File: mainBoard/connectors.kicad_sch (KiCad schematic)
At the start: 27 parts, among them J11 Conn_01x04, J12 Conn_01x05, J13 Conn_01x04, J14 Conn_01x06, J15 Conn_01x08, J16 Conn_01x03, J6 Conn_01x07, J7 Conn_01x04, J8 Conn_01x02, J9 Conn_01x02, Q2 IRLML6244TRPBF, Q3 IRLML6244TRPBF, Q4 IRLML6244TRPBF, Q5 IRLML6244TRPBF

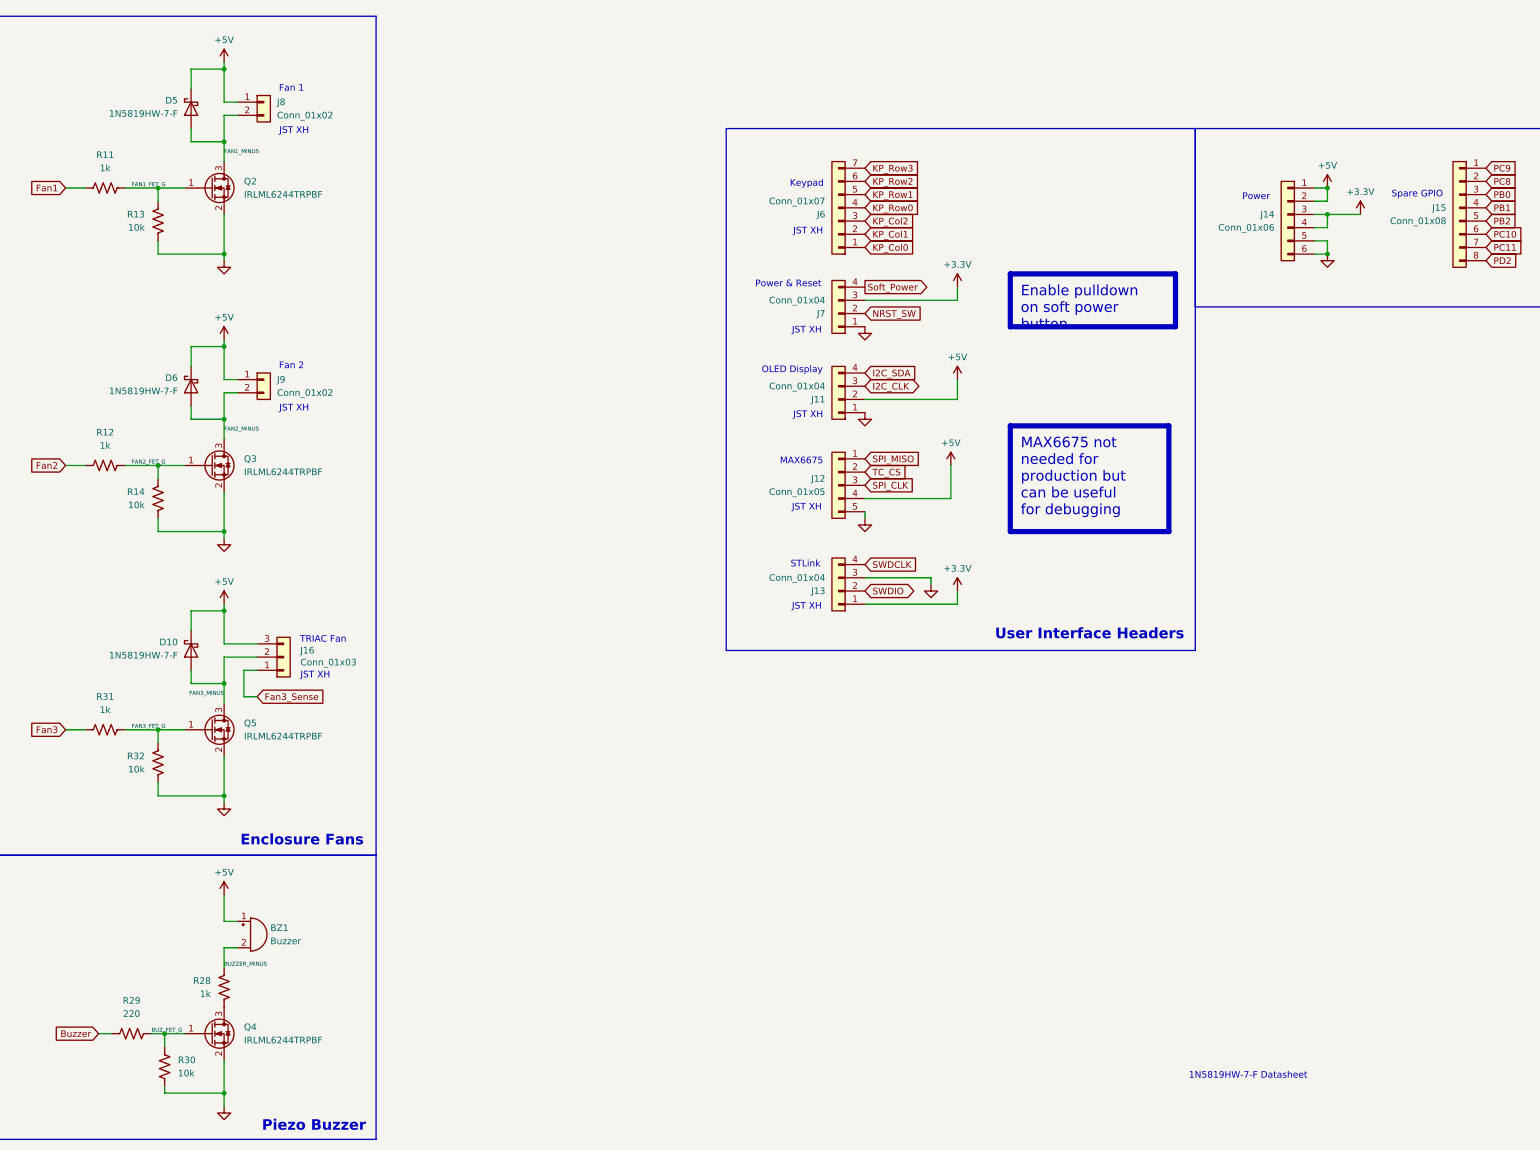
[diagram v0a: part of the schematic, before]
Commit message: Schematic Capture should be complete, ready for PCB
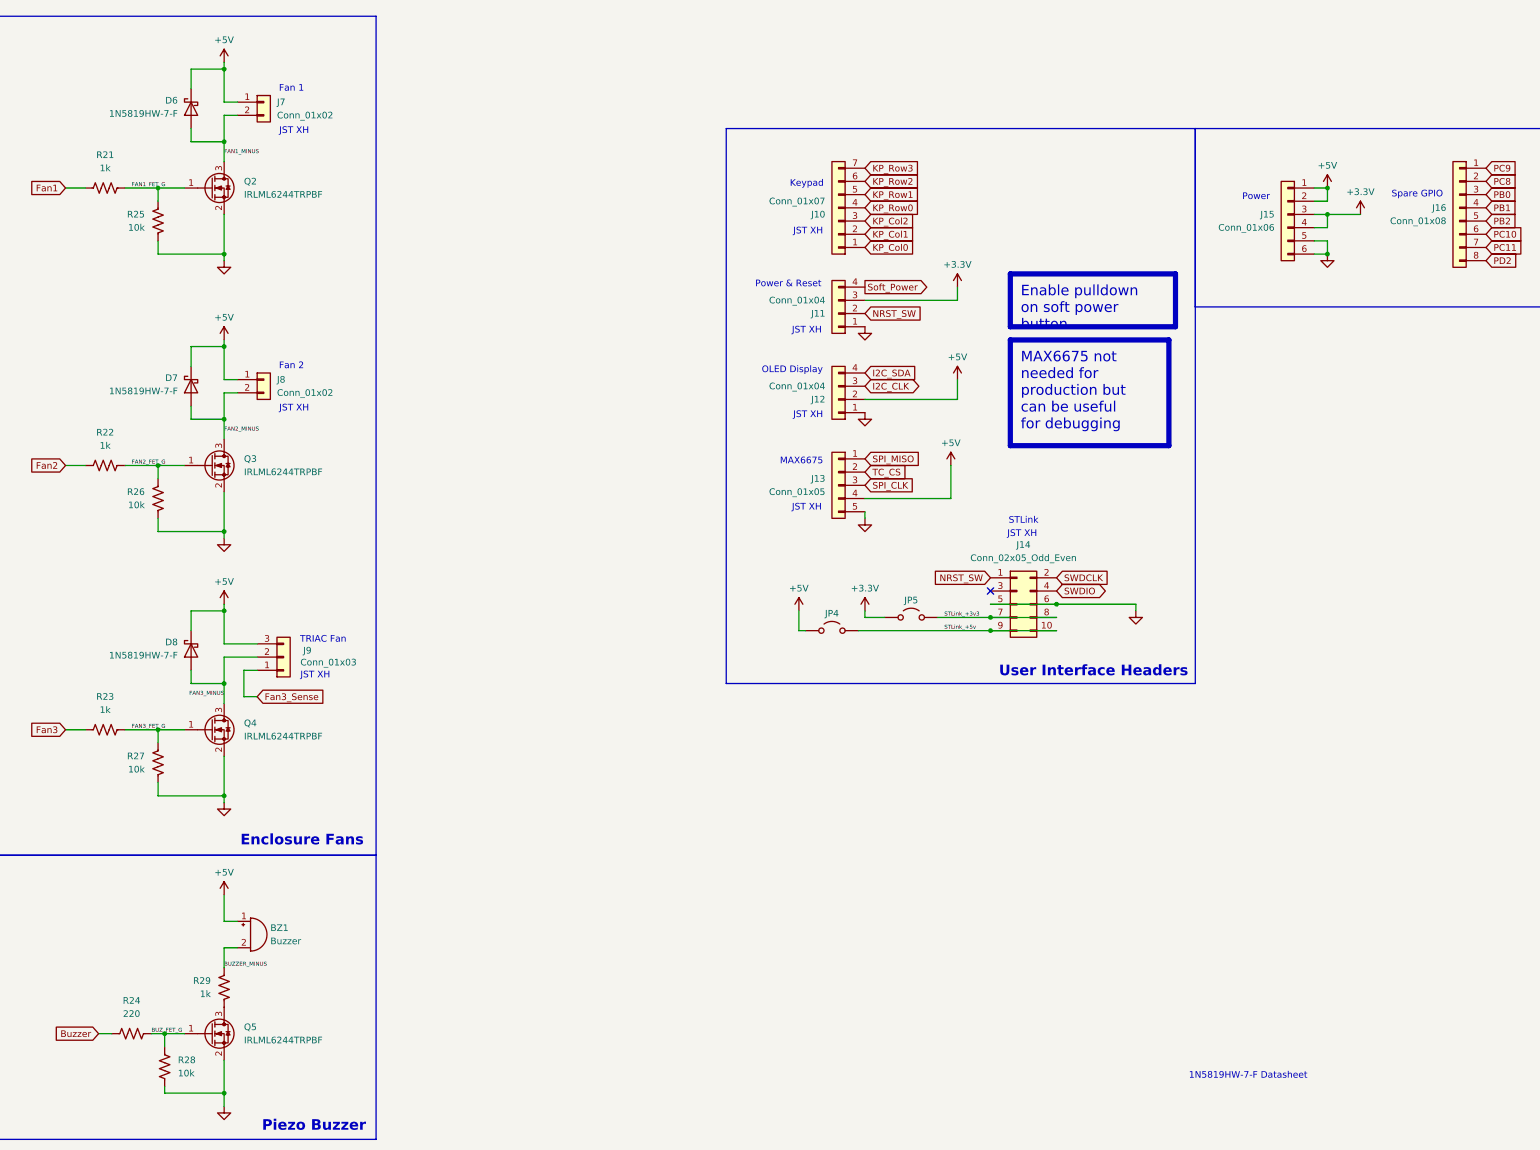
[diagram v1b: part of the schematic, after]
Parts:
- removed J13: Conn_01x04, Connector_JST:JST_XH_B4B-XH-A_1x04_P2.50mm_Vertical, symbol Connector_Generic:Conn_01x04
- added J14: Conn_02x05_Odd_Even, Connector_IDC:IDC-Header_2x05_P2.54mm_Vertical, symbol Connector_Generic:Conn_02x05_Odd_Even
- added JP4, JP5: Jumper_2_Open, Jumper:SolderJumper-2_P1.3mm_Open_TrianglePad1.0x1.5mm, symbol Jumper:Jumper_2_Open
- renumbered D5 to D6, D6 to D7, D10 to D8, J6 to J10, J7 to J11, J11 to J12, J12 to J13, J14 to J15, J15 to J16, J8 to J7, J9 to J8, J16 to J9, Q5 to Q4, Q4 to Q5, R11 to R21, R12 to R22, R31 to R23, R29 to R24, R13 to R25, R14 to R26, R32 to R27, R30 to R28, R28 to R29
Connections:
- net +3.3V: now also JP5.1 (A)
- net +5V: now also JP4.1 (A)
- net GND: now also J14.5 (Pin_5), J14.6 (Pin_6)
- net NRST_SW: now also J14.1 (Pin_1)
- net SWDCLK: now also J14.2 (Pin_2)
- net SWDIO: now also J14.4 (Pin_4)
- new net STLink_+3v3: J14.7 (Pin_7), J14.8 (Pin_8), JP5.2 (B)
- new net STLink_+5v: J14.10 (Pin_10), J14.9 (Pin_9), JP4.2 (B)
- no-connect marks 0 -> 1

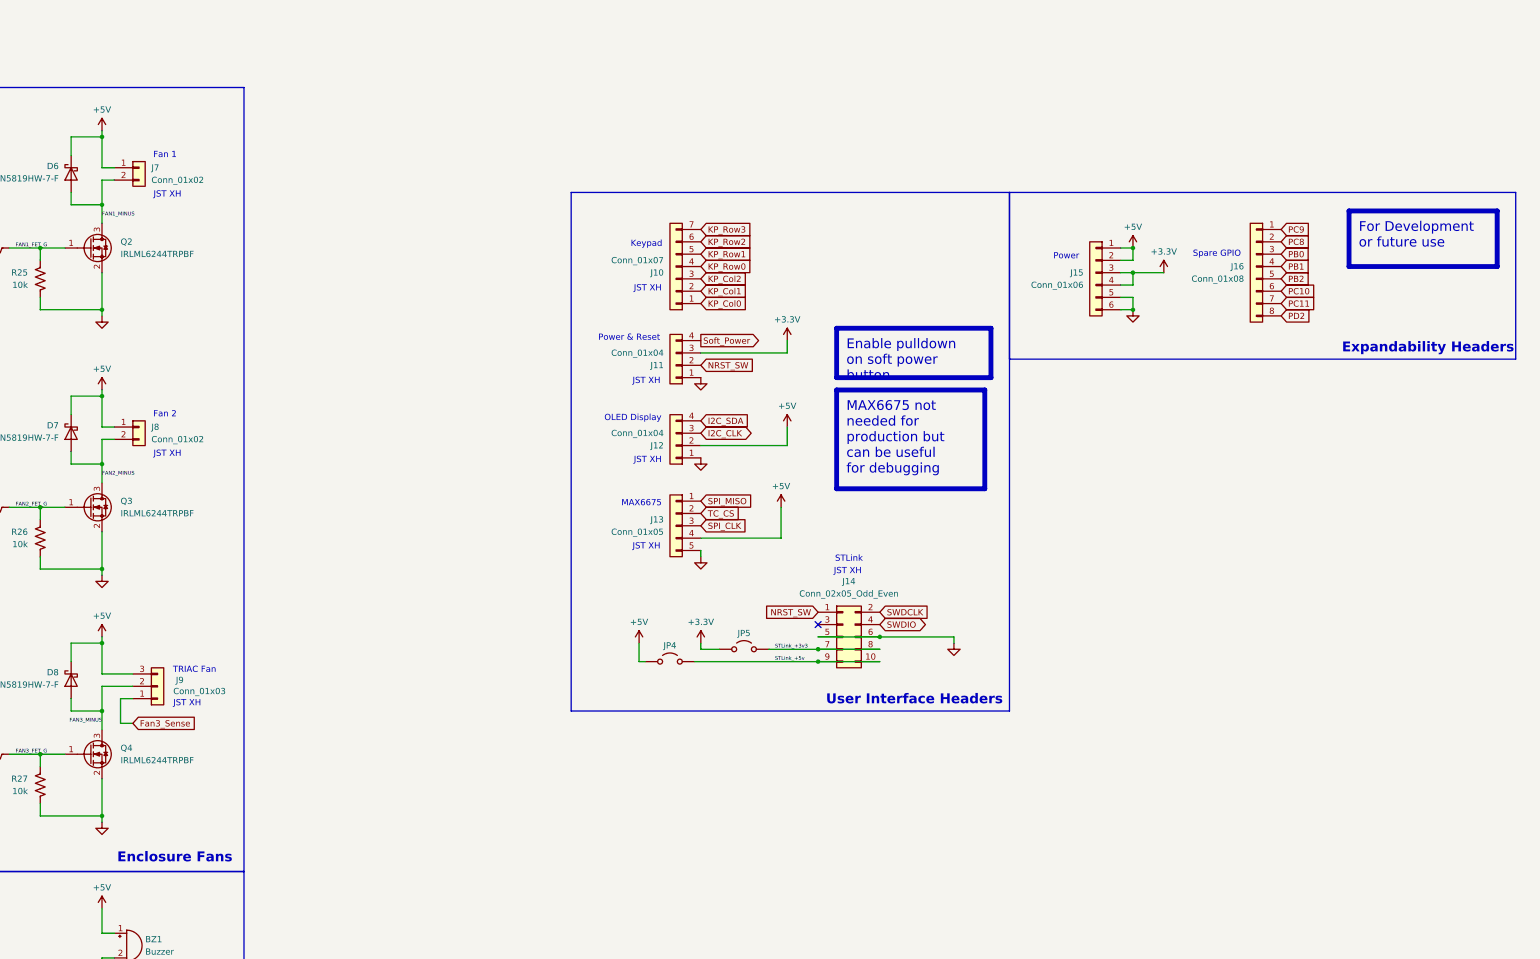
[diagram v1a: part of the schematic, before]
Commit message: tweak schematic for changes from 6-17-2026
major structural changes, see daily note from obsidian
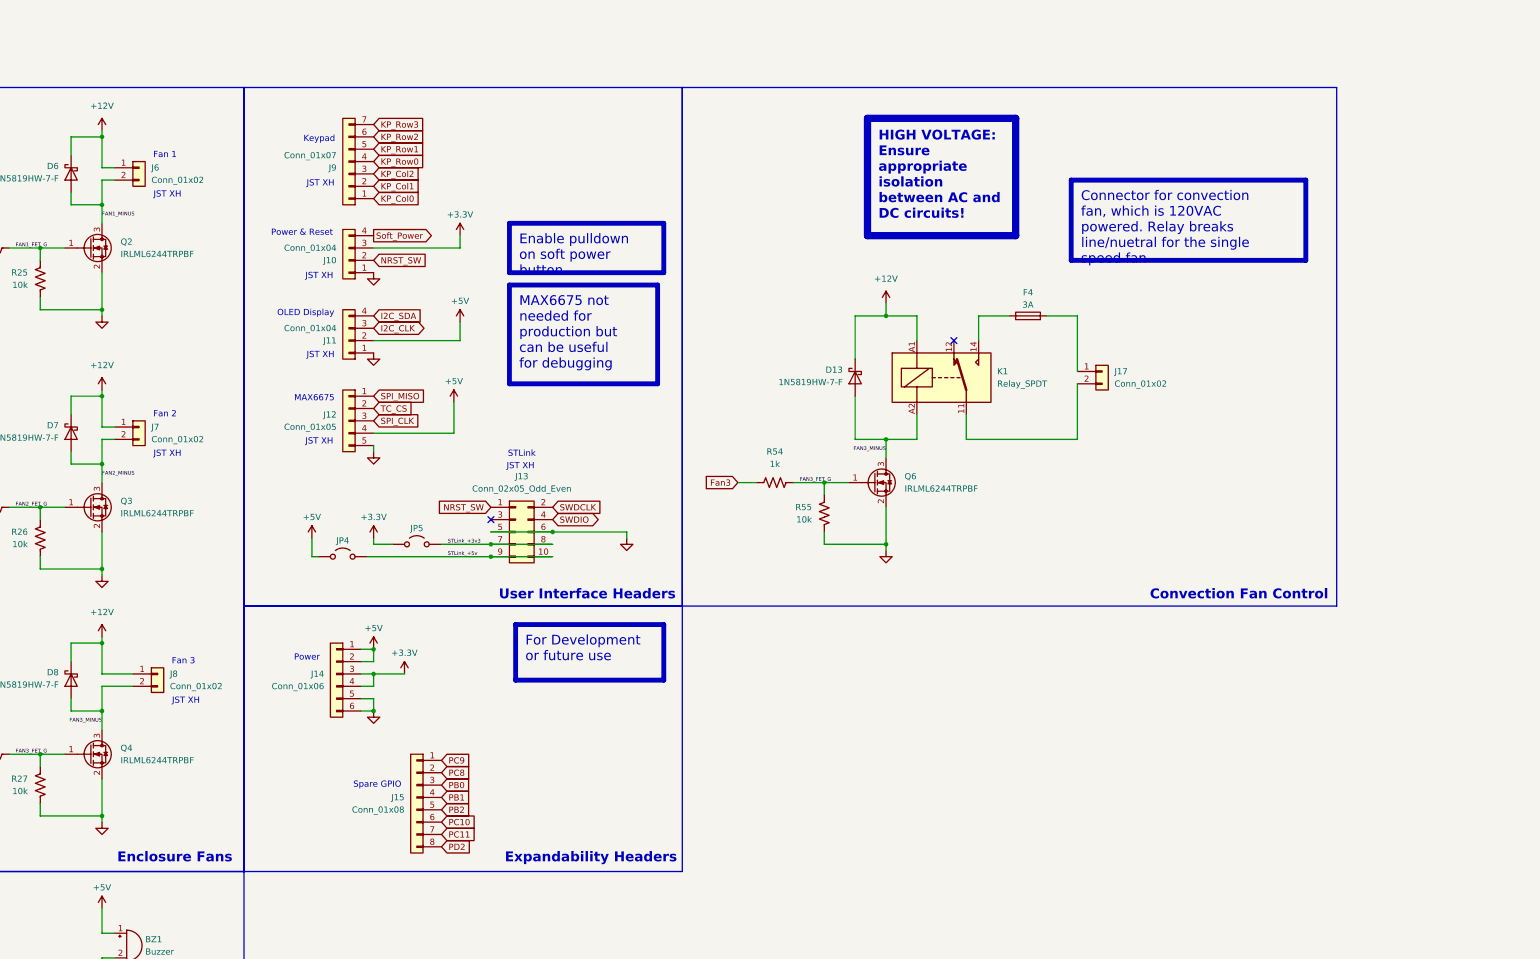
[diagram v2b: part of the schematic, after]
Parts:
- removed J9: Conn_01x03, Connector_JST:JST_XH_B3B-XH-A_1x03_P2.50mm_Vertical, symbol Connector_Generic:Conn_01x03
- added D13: 1N5819HW-7-F, Diode_SMD:D_SOD-123, symbol Diode:1N5819
- added F4: 3A, Fuse:Fuseholder_Clip-5x20mm_Littelfuse_100_Inline_P20.50x4.60mm_D1.30mm_Horizontal, symbol Device:Fuse
- added J17: Conn_01x02, TerminalBlock_Phoenix:TerminalBlock_Phoenix_MKDS-1,5-2-5.08_1x02_P5.08mm_Horizontal, symbol Connector_Generic:Conn_01x02
- added J8: Conn_01x02, Connector_JST:JST_XH_B2B-XH-A_1x02_P2.50mm_Vertical, symbol Connector_Generic:Conn_01x02
- added K1: Relay_SPDT, Relay_THT:Relay_SPDT_Finder_36.11, symbol Relay:Relay_SPDT
- added Q6: IRLML6244TRPBF, Package_TO_SOT_SMD:SOT-23, symbol Transistor_FET:IRLML6244
- added R54: 1k, Resistor_SMD:R_0603_1608Metric_Pad0.98x0.95mm_HandSolder, symbol Device:R_US
- added R55: 10k, Resistor_SMD:R_0603_1608Metric_Pad0.98x0.95mm_HandSolder, symbol Device:R_US
- J12: renamed from J13; now left out of the parts list
- renumbered J11 to J10, J12 to J11, J14 to J13, J15 to J14, J16 to J15, J7 to J6, J8 to J7, J10 to J9
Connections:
- net +5V: no longer D6.1 (K), D7.1 (K), D8.1 (K), J6.1 (Pin_1), J7.1 (Pin_1)
- net FAN3_FET_G: now also Q6.1 (G), R54.2, R55.1
- net FAN3_MINUS: now also D13.2 (A), J8.2 (Pin_2), K1.A2, Q6.3 (D)
- net Fan3: now also R54.1
- net GND: now also Q6.2 (S), R55.2
- new net: F4.2, J17.1 (Pin_1)
- new net: J17.2 (Pin_2), K1.11
- new net: F4.1, K1.14
- new net +12V: D13.1 (K), D6.1 (K), D7.1 (K), D8.1 (K), J6.1 (Pin_1), J7.1 (Pin_1), J8.1 (Pin_1), K1.A1
- no-connect marks 1 -> 2
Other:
- note added: "Convection Fan Control"
- note added: "Fan 3"
- note removed: "TRIAC Fan"
- moved on the sheet: J10, J11, J12, J13, J14, J15, J9, JP4, JP5

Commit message: working on pcb layout after bringing in work from laptop
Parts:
- removed J12: Conn_01x05, Connector_JST:JST_XH_B5B-XH-A_1x05_P2.50mm_Vertical, symbol Connector_Generic:Conn_01x05
- removed J15: Conn_01x08, Connector_PinHeader_2.54mm:PinHeader_1x08_P2.54mm_Vertical, symbol Connector_Generic:Conn_01x08
- added D15: RED, LED_SMD:LED_0603_1608Metric_Pad1.05x0.95mm_HandSolder, symbol Device:LED_Filled
- added J17: Conn_01x06, Connector_PinHeader_2.54mm:PinHeader_1x06_P2.54mm_Vertical, symbol Connector_Generic:Conn_01x06
- added R59: 1k, Resistor_SMD:R_0603_1608Metric_Pad0.98x0.95mm_HandSolder, symbol Device:R_US
- renumbered D6 to D10, D7 to D11, D8 to D12, J14 to J10, J9 to J11, J10 to J12, J11 to J13, J13 to J15, J17 to J16, J6 to J7, J7 to J8, J8 to J9, JP4 to JP8, JP5 to JP9, Q2 to Q3, Q3 to Q4, Q4 to Q5, Q5 to Q6, Q6 to Q7, R21 to R47, R22 to R48, R23 to R49, R24 to R50, R25 to R51, R26 to R52, R27 to R53, R28 to R54, R29 to R55, R54 to R56, R55 to R57
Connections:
- net +12V: now also D15.2 (A)
- net +3.3V: now also J10.5 (Pin_5), J10.6 (Pin_6); no longer J10.3 (Pin_3), J10.4 (Pin_4)
- net FAN3_FET_G: no longer Q7.1 (G), R56.2, R57.1
- net FAN3_MINUS: no longer D13.2 (A), K1.A2, Q7.3 (D)
- net Fan3: no longer R56.1
- net GND: now also J10.3 (Pin_3), J10.4 (Pin_4); no longer J10.5 (Pin_5), J10.6 (Pin_6)
- net PB0: now also J17.6 (Pin_6)
- net PB1: now also J17.5 (Pin_5)
- net PB2: now also J17.4 (Pin_4)
- net PC8: now also J17.2 (Pin_2)
- net PC9: now also J17.3 (Pin_3)
- net CONVFAN_L1: now reaches F4.2, J16.1 (Pin_1)
- net CONVFAN_L1_SW: now reaches J16.2 (Pin_2), K1.11
- net CONVFAN_L1_FUSED: now reaches F4.1, K1.14
- new net CONVFAN_FET_G: Q7.1 (G), R56.2, R57.1
- new net CONVFAN_RELAY_MINUS: D13.2 (A), K1.A2, Q7.3 (D), R59.2
- new net Conv_Fan: R56.1
- new net D15_K: D15.1 (K), R59.1
- no-connect marks 2 -> 3
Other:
- note removed: "MAX6675"
- moved on the sheet: D13, F4, J10, J11, J12, J13, J16, K1, Q7, R56, R57
